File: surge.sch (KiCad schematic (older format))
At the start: 1 part

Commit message: r
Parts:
- removed X?: IEC_power, symbol IEC_power
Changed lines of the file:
@@
 EELAYER 25 0
 EELAYER END
-$Descr A3 16535 11693
+$Descr A4 11693 8268
 encoding utf-8
-Sheet 1 2
+Sheet 2 2
 Title ""
 Date ""
@@
 Comment4 ""
 $EndDescr
-$Sheet
-S 1425 725  875  525
-U 5882A13F
-F0 "surge" 60
-F1 "surge.sch" 60
-F2 "L_I" I L 1425 900 60
-F3 "PE_I" O L 1425 975 60
-F4 "N_I" O L 1425 1050 60
-F5 "L_O" O R 2300 900 60
-F6 "PE_O" I R 2300 975 60
-F7 "N_O" I R 2300 1050 60
-$EndSheet
-$Comp
-L IEC_power X?
-U 1 1 5882AB14
-P 675 1075
-F 0 "X?" H 725 1375 60  0000 C CNN
-F 1 "IEC_power" H 900 1025 60  0000 C CNN
-F 2 "" H 675 1075 60  0001 C CNN
-F 3 "" H 675 1075 60  0001 C CNN
-	1    675  1075
-	1    0    0    -1
-$EndComp
+Text HLabel 1900 2775 0    60   Input ~ 0
+L_I
+Text HLabel 1900 2850 0    60   Output ~ 0
+PE_I
+Text HLabel 1900 2925 0    60   Output ~ 0
+N_I
 Wire Wire Line
-	1125 900  1425 900
+	1900 2775 7325 2775
 Wire Wire Line
-	1175 975  1425 975
+	1900 2850 7325 2850
 Wire Wire Line
-	1175 1050 1425 1050
+	1900 2925 7325 2925
+Text HLabel 7325 2775 2    60   Output ~ 0
+L_O
+Text HLabel 7325 2850 2    60   Input ~ 0
+PE_O
+Text HLabel 7325 2925 2    60   Input ~ 0
+N_O
 $EndSCHEMATC

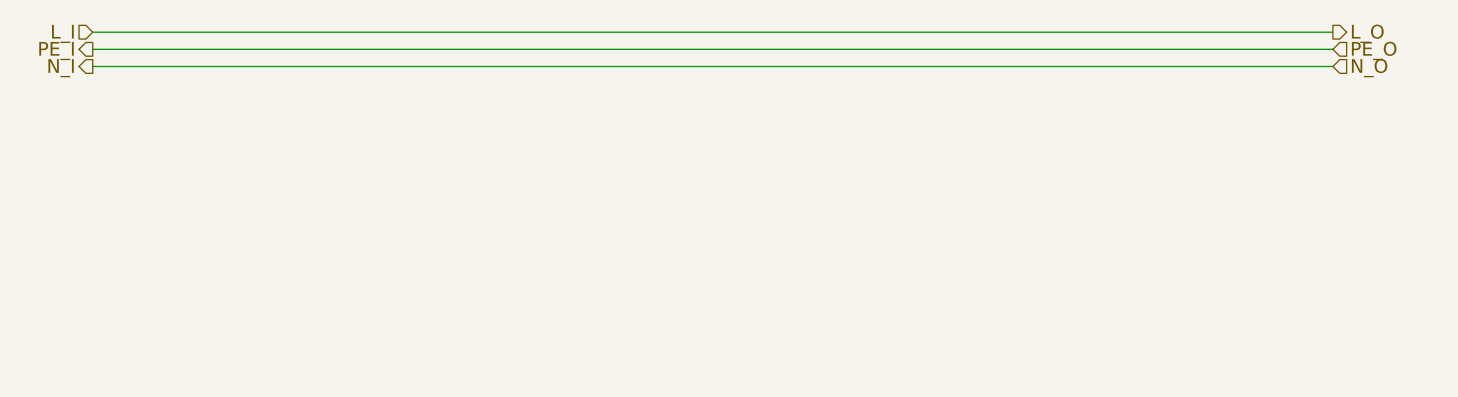
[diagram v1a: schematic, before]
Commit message: surge protection from ac net
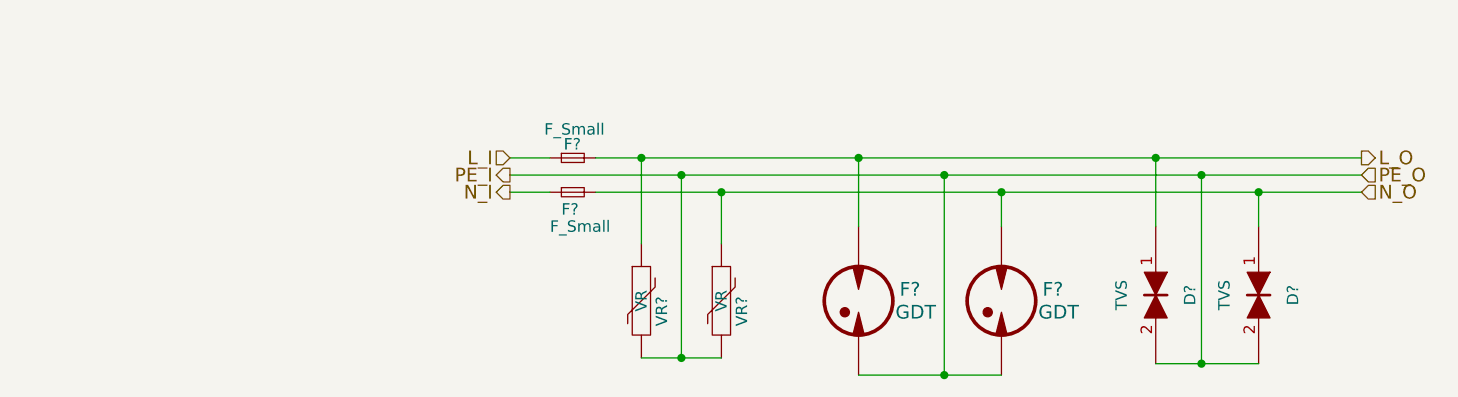
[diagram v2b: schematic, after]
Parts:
- added D? (x2): TVS, symbol TVS
- added F? (x2): GDT, symbol GDT
- added F? (x2): F_Small, symbol F_Small
- added VR? (x2): VR, symbol VR
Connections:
- net L_I: now also F?.1
- net N_I: now also F?.1
- net PE_I: now also D?.2, D?.2, F?.~, F?.~, VR?.2, VR?.2
- new net L_O: D?.1, F?.2, F?.~, VR?.1
- new net N_O: D?.1, F?.2, F?.~, VR?.1
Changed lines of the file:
@@
 LIBS:valves
 LIBS:selfmade
+LIBS:preamp-cache
 EELAYER 25 0
 EELAYER END
@@
 Comment4 ""
 $EndDescr
-Text HLabel 1900 2775 0    60   Input ~ 0
+Text HLabel 3725 3325 0    60   Input ~ 0
 L_I
-Text HLabel 1900 2850 0    60   Output ~ 0
+Text HLabel 3725 3400 0    60   Output ~ 0
 PE_I
-Text HLabel 1900 2925 0    60   Output ~ 0
+Text HLabel 3725 3475 0    60   Output ~ 0
 N_I
 Wire Wire Line
-	1900 2775 7325 2775
+	4100 3325 4300 3325
 Wire Wire Line
-	1900 2850 7325 2850
+	4300 3325 5250 3325
 Wire Wire Line
-	1900 2925 7325 2925
-Text HLabel 7325 2775 2    60   Output ~ 0
+	5250 3325 6550 3325
+Wire Wire Line
+	6550 3325 7450 3325
+Wire Wire Line
+	3725 3400 4475 3400
+Wire Wire Line
+	4475 3400 5625 3400
+Wire Wire Line
+	5625 3400 6750 3400
+Wire Wire Line
+	6750 3400 7450 3400
+Wire Wire Line
+	4100 3475 4650 3475
+Wire Wire Line
+	4650 3475 5875 3475
+Wire Wire Line
+	5875 3475 7000 3475
+Wire Wire Line
+	7000 3475 7450 3475
+Text HLabel 7450 3325 2    60   Output ~ 0
 L_O
-Text HLabel 7325 2850 2    60   Input ~ 0
+Text HLabel 7450 3400 2    60   Input ~ 0
 PE_O
-Text HLabel 7325 2925 2    60   Input ~ 0
+Text HLabel 7450 3475 2    60   Input ~ 0
 N_O
+$Comp
+L GDT F?
+U 1 1 58834DC5
+P 5250 3950
+F 0 "F?" H 5475 4000 60  0000 C CNN
+F 1 "GDT" H 5500 3900 60  0000 C CNN
+F 2 "" H 5250 3950 60  0001 C CNN
+F 3 "" H 5250 3950 60  0001 C CNN
+	1    5250 3950
+	1    0    0    -1
+$EndComp
+$Comp
+L VR VR?
+U 1 1 58834E08
+P 4300 3950
+F 0 "VR?" V 4360 3904 50  0000 C TNN
+F 1 "VR" V 4300 3950 50  0000 C CNN
+F 2 "" H 4300 3950 50  0000 C CNN
+F 3 "" H 4300 3950 50  0000 C CNN
+	1    4300 3950
+	1    0    0    -1
+$EndComp
+Wire Wire Line
+	4300 3700 4300 3325
+Connection ~ 4300 3325
+Wire Wire Line
+	5250 3625 5250 3325
+Connection ~ 5250 3325
+Wire Wire Line
+	5625 3400 5625 4275
+Wire Wire Line
+	5250 4275 5625 4275
+Wire Wire Line
+	5625 4275 5875 4275
+Connection ~ 5625 3400
+$Comp
+L GDT F?
+U 1 1 58834F79
+P 5875 3950
+F 0 "F?" H 6100 4000 60  0000 C CNN
+F 1 "GDT" H 6125 3900 60  0000 C CNN
+F 2 "" H 5875 3950 60  0001 C CNN
+F 3 "" H 5875 3950 60  0001 C CNN
+	1    5875 3950
+	1    0    0    -1
+$EndComp
+Wire Wire Line
+	5875 3625 5875 3475
+Connection ~ 5875 3475
+Connection ~ 5625 4275
+$Comp
+L VR VR?
+U 1 1 58834FE0
+P 4650 3950
+F 0 "VR?" V 4710 3904 50  0000 C TNN
+F 1 "VR" V 4650 3950 50  0000 C CNN
+F 2 "" H 4650 3950 50  0000 C CNN
+F 3 "" H 4650 3950 50  0000 C CNN
+	1    4650 3950
+	1    0    0    -1
+$EndComp
+Wire Wire Line
+	4650 3700 4650 3475
+Connection ~ 4650 3475
+Wire Wire Line
+	4300 4200 4475 4200
+Wire Wire Line
+	4475 4200 4650 4200
+Wire Wire Line
+	4475 4200 4475 3400
+Connection ~ 4475 3400
+Connection ~ 4475 4200
+$Comp
+L F_Small F?
+U 1 1 5883569D
+P 4000 3325
+F 0 "F?" H 3960 3385 50  0000 L CNN
+F 1 "F_Small" H 3875 3450 50  0000 L CNN
+F 2 "" H 4000 3325 50  0000 C CNN
+F 3 "" H 4000 3325 50  0000 C CNN
+	1    4000 3325
+	1    0    0    -1
+$EndComp
+$Comp
+L F_Small F?
+U 1 1 588356F2
+P 4000 3475
+F 0 "F?" H 3950 3400 50  0000 L CNN
+F 1 "F_Small" H 3900 3325 50  0000 L CNN
+F 2 "" H 4000 3475 50  0000 C CNN
+F 3 "" H 4000 3475 50  0000 C CNN
+	1    4000 3475
+	1    0    0    -1
+$EndComp
+Wire Wire Line
+	3725 3325 3900 3325
+Wire Wire Line
+	3900 3475 3725 3475
+$Comp
+L TVS D?
+U 1 1 58835ECA
+P 6550 3925
+F 0 "D?" H 6550 4075 50  0000 C CNN
+F 1 "TVS" H 6550 3775 50  0000 C CNN
+F 2 "" H 6550 3925 50  0000 C CNN
+F 3 "" H 6550 3925 50  0000 C CNN
+	1    6550 3925
+	0    1    1    0
+$EndComp
+$Comp
+L TVS D?
+U 1 1 58835F26
+P 7000 3925
+F 0 "D?" H 7000 4075 50  0000 C CNN
+F 1 "TVS" H 7000 3775 50  0000 C CNN
+F 2 "" H 7000 3925 50  0000 C CNN
+F 3 "" H 7000 3925 50  0000 C CNN
+	1    7000 3925
+	0    1    1    0
+$EndComp
+Wire Wire Line
+	6550 4225 6750 4225
+Wire Wire Line
+	6750 4225 7000 4225
+Wire Wire Line
+	6750 4225 6750 3400
+Connection ~ 6750 3400
+Wire Wire Line
+	6550 3625 6550 3325
+Connection ~ 6550 3325
+Wire Wire Line
+	7000 3625 7000 3475
+Connection ~ 7000 3475
+Connection ~ 6750 4225
 $EndSCHEMATC
